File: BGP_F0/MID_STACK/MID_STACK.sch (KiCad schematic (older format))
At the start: 6 parts, among them P1 CONN_01X04, P2 CONN_01X09

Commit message: BT and MID pot gain ctrl reversed for proper action
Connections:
- net MID_I: now also P2.3 (P3); no longer P2.1 (P1)
- net MID_O: now also P2.1 (P1); no longer P2.3 (P3)
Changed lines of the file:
@@
 Comment4 ""
 $EndDescr
-Text Label 5500 3550 2    60   ~ 0
+Text Label 5500 3350 2    60   ~ 0
 VOL1
 Text Label 5500 3450 2    60   ~ 0
 VOL2
-Text Label 5500 3350 2    60   ~ 0
+Text Label 5500 3550 2    60   ~ 0
 VOL3
 Wire Wire Line

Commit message: Mid Buff
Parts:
- R1, R2: value 12k -> 6.8k
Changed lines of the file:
@@
 Text Label 5500 3550 2    60   ~ 0
 VOL3
-Wire Wire Line
-	5500 3450 5550 3450
 $Comp
 L C_Small C1
@@
 P 5900 3450
 F 0 "R1" H 5930 3470 50  0000 L CNN
-F 1 "12k" H 5930 3410 50  0000 L CNN
+F 1 "6.8k" H 5930 3410 50  0000 L CNN
 F 2 "Resistors_SMD:R_0603_HandSoldering" H 5900 3450 50  0001 C CNN
 F 3 "" H 5900 3450 50  0000 C CNN
@@
 	0    -1   -1   0
 $EndComp
-Wire Wire Line
-	5800 3450 5750 3450
-Wire Wire Line
-	6000 3450 6050 3450
 Text Label 6050 3450 3    60   ~ 0
 F1_2
 Text Label 6150 3450 3    60   ~ 0
 F1_1
-Wire Wire Line
-	6250 3450 6250 3900
-Wire Wire Line
-	6250 4000 6250 4050
 $Comp
 L R_Small R2
@@
 P 6250 4150
 F 0 "R2" H 6280 4170 50  0000 L CNN
-F 1 "12k" H 6280 4110 50  0000 L CNN
+F 1 "6.8k" H 6280 4110 50  0000 L CNN
 F 2 "Resistors_SMD:R_0603_HandSoldering" H 6250 4150 50  0001 C CNN
 F 3 "" H 6250 4150 50  0000 C CNN
@@
 	1    0    0    -1
 $EndComp
-Connection ~ 6250 3800
-Wire Wire Line
-	6250 4250 6250 4350
-Wire Wire Line
-	6250 4300 5950 4300
-Wire Wire Line
-	5950 4300 5950 4250
-Wire Wire Line
-	5950 4050 5950 3800
-Wire Wire Line
-	5950 3800 6250 3800
-Connection ~ 6250 4300
 Text Label 6900 3650 2    60   ~ 0
 VOL1
@@
 Text Label 6900 4350 2    60   ~ 0
 F2_2
-Wire Wire Line
-	6900 4150 6900 4050
-Wire Wire Line
-	6900 4450 6900 4350
-Wire Wire Line
-	6250 3450 6150 3450
-Wire Wire Line
-	5500 3200 5500 3350
-Wire Wire Line
-	5500 3650 5500 3550
 Text Label 6250 4350 3    60   ~ 0
 Vref
@@
 Text Label 5000 3900 0    60   ~ 0
 MID_I
+Wire Wire Line
+	5500 3450 5550 3450
+Wire Wire Line
+	5800 3450 5750 3450
+Wire Wire Line
+	6000 3450 6050 3450
+Wire Wire Line
+	6250 3450 6250 3900
+Wire Wire Line
+	6250 4000 6250 4050
+Connection ~ 6250 3800
+Wire Wire Line
+	6250 4250 6250 4350
+Wire Wire Line
+	6250 4300 5950 4300
+Wire Wire Line
+	5950 4300 5950 4250
+Wire Wire Line
+	5950 4050 5950 3800
+Wire Wire Line
+	5950 3800 6250 3800
+Connection ~ 6250 4300
+Wire Wire Line
+	6900 4150 6900 4050
+Wire Wire Line
+	6900 4450 6900 4350
+Wire Wire Line
+	6250 3450 6150 3450
+Wire Wire Line
+	5500 3200 5500 3350
+Wire Wire Line
+	5500 3650 5500 3550
 $EndSCHEMATC

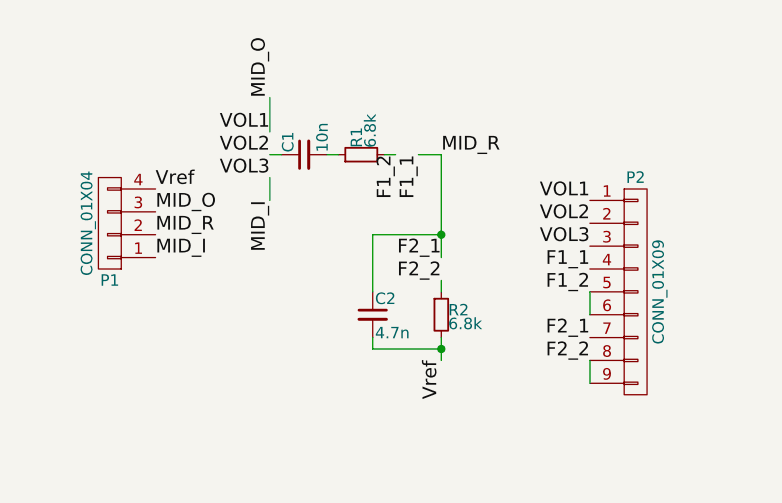
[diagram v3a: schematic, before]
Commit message: Change some caps to TH, updated BOM - need to recreate
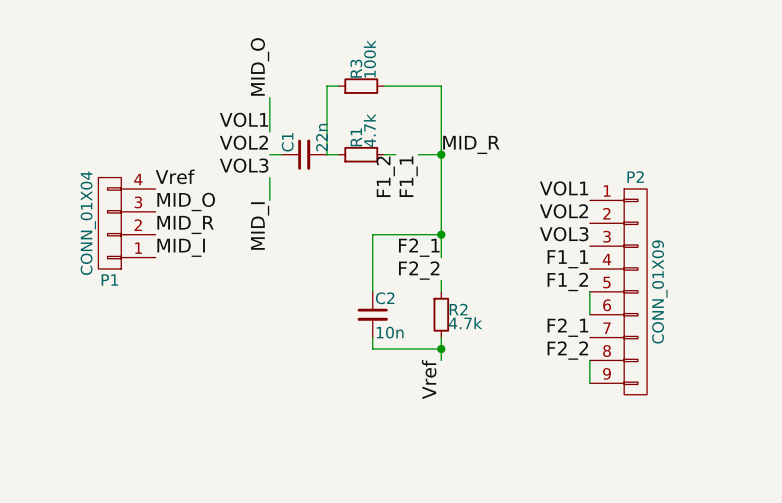
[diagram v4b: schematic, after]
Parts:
- added R3: 100k, Resistors_SMD:R_0603_HandSoldering, symbol R_Small
- C1: value 10n -> 22n; footprint Capacitors_SMD:C_0805_HandSoldering -> Capacitor_THT:C_Rect_L7.2mm_W2.5mm_P5.00mm_FKS2_FKP2_MKS2_MKP2
- C2: value 4.7n -> 10n; footprint Capacitors_SMD:C_0805_HandSoldering -> Capacitor_THT:C_Rect_L7.2mm_W2.5mm_P5.00mm_FKS2_FKP2_MKS2_MKP2
- R1, R2: value 6.8k -> 4.7k
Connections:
- net F1_1: now also R3.2
- net at C1.2, R1.1: now also R3.1
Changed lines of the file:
@@
 P 5650 3450
 F 0 "C1" H 5660 3520 50  0000 L CNN
-F 1 "10n" H 5660 3370 50  0000 L CNN
-F 2 "Capacitors_SMD:C_0805_HandSoldering" H 5650 3450 50  0001 C CNN
+F 1 "22n" H 5660 3370 50  0000 L CNN
+F 2 "Capacitor_THT:C_Rect_L7.2mm_W2.5mm_P5.00mm_FKS2_FKP2_MKS2_MKP2" H 5650 3450 50  0001 C CNN
 F 3 "" H 5650 3450 50  0000 C CNN
 	1    5650 3450
@@
 P 5900 3450
 F 0 "R1" H 5930 3470 50  0000 L CNN
-F 1 "6.8k" H 5930 3410 50  0000 L CNN
+F 1 "4.7k" H 5930 3410 50  0000 L CNN
 F 2 "Resistors_SMD:R_0603_HandSoldering" H 5900 3450 50  0001 C CNN
 F 3 "" H 5900 3450 50  0000 C CNN
@@
 P 6250 4150
 F 0 "R2" H 6280 4170 50  0000 L CNN
-F 1 "6.8k" H 6280 4110 50  0000 L CNN
+F 1 "4.7k" H 6280 4110 50  0000 L CNN
 F 2 "Resistors_SMD:R_0603_HandSoldering" H 6250 4150 50  0001 C CNN
 F 3 "" H 6250 4150 50  0000 C CNN
@@
 P 5950 4150
 F 0 "C2" H 5960 4220 50  0000 L CNN
-F 1 "4.7n" H 5960 4070 50  0000 L CNN
-F 2 "Capacitors_SMD:C_0805_HandSoldering" H 5950 4150 50  0001 C CNN
+F 1 "10n" H 5960 4070 50  0000 L CNN
+F 2 "Capacitor_THT:C_Rect_L7.2mm_W2.5mm_P5.00mm_FKS2_FKP2_MKS2_MKP2" H 5950 4150 50  0001 C CNN
 F 3 "" H 5950 4150 50  0000 C CNN
 	1    5950 4150
@@
 	6000 3450 6050 3450
 Wire Wire Line
-	6250 3450 6250 3900
+	6250 3150 6250 3900
 Wire Wire Line
 	6250 4000 6250 4050
@@
 Wire Wire Line
 	5500 3650 5500 3550
+$Comp
+L R_Small R3
+U 1 1 5A88CD87
+P 5900 3150
+F 0 "R3" H 5930 3170 50  0000 L CNN
+F 1 "100k" H 5930 3110 50  0000 L CNN
+F 2 "Resistors_SMD:R_0603_HandSoldering" H 5900 3150 50  0001 C CNN
+F 3 "" H 5900 3150 50  0000 C CNN
+	1    5900 3150
+	0    -1   -1   0
+$EndComp
+Wire Wire Line
+	5750 3450 5750 3150
+Wire Wire Line
+	5750 3150 5800 3150
+Wire Wire Line
+	6000 3150 6250 3150
+Connection ~ 6250 3450
 $EndSCHEMATC

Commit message: F0 Mid Stack fixed
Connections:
- net F1_1: now also P2.1 (P1); no longer P2.7 (P7)
- net F1_2: now also P2.2 (P2), P2.3 (P3); no longer P2.5 (P5), P2.6 (P6)
- net F2_2: now also P2.5 (P5), P2.6 (P6); no longer P2.8 (P8), P2.9 (P9)
- net MID_I: now also P2.9 (P9); no longer P2.3 (P3)
- net MID_O: now also P2.7 (P7); no longer P2.1 (P1)
- net VOL2: now also P2.8 (P8); no longer P2.2 (P2)
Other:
- moved on the sheet: P1, P2
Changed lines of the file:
@@
 	1    0    0    -1
 $EndComp
-Text Label 6900 3650 2    60   ~ 0
+Text Label 6950 3750 2    60   ~ 0
 VOL1
-Text Label 6900 3750 2    60   ~ 0
+Text Label 6950 3850 2    60   ~ 0
 VOL2
-Text Label 6900 3850 2    60   ~ 0
+Text Label 6950 3950 2    60   ~ 0
 VOL3
-Text Label 6900 3950 2    60   ~ 0
+Text Label 6950 3150 2    60   ~ 0
 F1_1
-Text Label 6900 4050 2    60   ~ 0
+Text Label 6950 3250 2    60   ~ 0
 F1_2
-Text Label 6900 4250 2    60   ~ 0
+Text Label 6950 3450 2    60   ~ 0
 F2_1
-Text Label 6900 4350 2    60   ~ 0
+Text Label 6950 3550 2    60   ~ 0
 F2_2
 Text Label 6250 4350 3    60   ~ 0
@@
 L CONN_01X09 P2
 U 1 1 5A669FB9
-P 7100 4050
-F 0 "P2" H 7100 4550 50  0000 C CNN
-F 1 "CONN_01X09" V 7200 4050 50  0000 C CNN
-F 2 "LIBS:Potentiometer_Alpha_Tripple_Vertical_Dual_Shaft" H 7100 4050 50  0001 C CNN
-F 3 "" H 7100 4050 50  0000 C CNN
-	1    7100 4050
+P 7150 3550
+F 0 "P2" H 7150 4050 50  0000 C CNN
+F 1 "CONN_01X09" V 7250 3550 50  0000 C CNN
+F 2 "LIBS:Potentiometer_Alpha_Tripple_Vertical_Dual_Shaft" H 7150 3550 50  0001 C CNN
+F 3 "" H 7150 3550 50  0000 C CNN
+	1    7150 3550
 	1    0    0    -1
 $EndComp
@@
 L CONN_01X04 P1
 U 1 1 5A66A01B
-P 4800 3750
-F 0 "P1" H 4800 4000 50  0000 C CNN
-F 1 "CONN_01X04" V 4900 3750 50  0000 C CNN
-F 2 "Connectors_JST:JST_PH_B4B-PH-K_04x2.00mm_Straight" H 4800 3750 50  0001 C CNN
-F 3 "" H 4800 3750 50  0000 C CNN
-	1    4800 3750
+P 4550 3300
+F 0 "P1" H 4550 3550 50  0000 C CNN
+F 1 "CONN_01X04" V 4650 3300 50  0000 C CNN
+F 2 "Connectors_JST:JST_PH_B4B-PH-K_04x2.00mm_Straight" H 4550 3300 50  0001 C CNN
+F 3 "" H 4550 3300 50  0000 C CNN
+	1    4550 3300
 	-1   0    0    1
 $EndComp
-Text Label 5000 3600 0    60   ~ 0
+Text Label 4750 3150 0    60   ~ 0
 Vref
-Text Label 5000 3700 0    60   ~ 0
+Text Label 4750 3250 0    60   ~ 0
 MID_O
-Text Label 5000 3800 0    60   ~ 0
+Text Label 4750 3350 0    60   ~ 0
 MID_R
-Text Label 5000 3900 0    60   ~ 0
+Text Label 4750 3450 0    60   ~ 0
 MID_I
 Wire Wire Line
@@
 Connection ~ 6250 4300
 Wire Wire Line
-	6900 4150 6900 4050
+	6950 3350 6950 3250
 Wire Wire Line
-	6900 4450 6900 4350
+	6950 3650 6950 3550
 Wire Wire Line
 	6250 3450 6150 3450

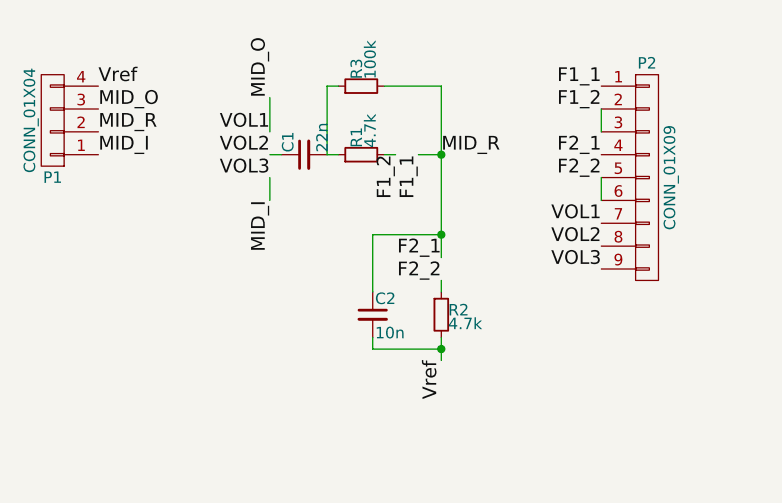
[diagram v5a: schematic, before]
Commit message: F0 Pot Wiring reversed after testing
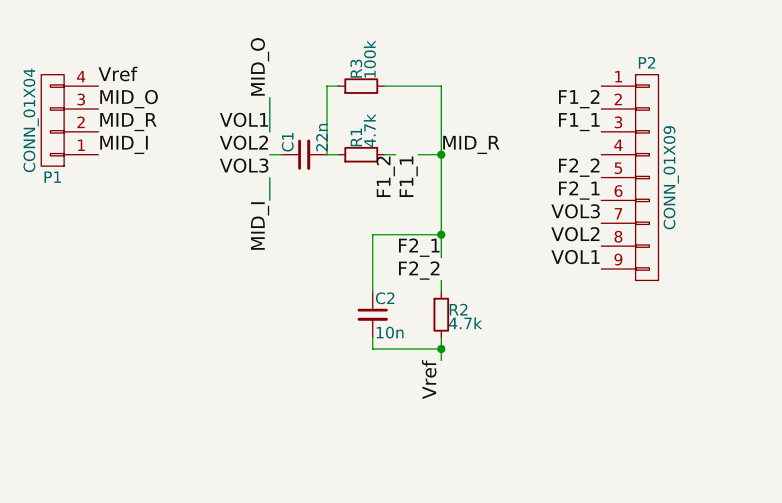
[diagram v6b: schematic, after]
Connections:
- net F1_1: now also P2.3 (P3), P2.6 (P6); no longer P2.1 (P1), P2.4 (P4)
- net F1_2: no longer P2.3 (P3)
- net F2_2: no longer P2.6 (P6)
- net MID_I: now also P2.7 (P7); no longer P2.9 (P9)
- net MID_O: now also P2.9 (P9); no longer P2.7 (P7)
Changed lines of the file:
@@
 	1    0    0    -1
 $EndComp
-Text Label 6950 3750 2    60   ~ 0
+Text Label 6950 3950 2    60   ~ 0
 VOL1
 Text Label 6950 3850 2    60   ~ 0
 VOL2
-Text Label 6950 3950 2    60   ~ 0
+Text Label 6950 3750 2    60   ~ 0
 VOL3
-Text Label 6950 3150 2    60   ~ 0
+Text Label 6950 3350 2    60   ~ 0
 F1_1
 Text Label 6950 3250 2    60   ~ 0
 F1_2
-Text Label 6950 3450 2    60   ~ 0
+Text Label 6950 3650 2    60   ~ 0
 F2_1
 Text Label 6950 3550 2    60   ~ 0
@@
 Connection ~ 6250 4300
 Wire Wire Line
-	6950 3350 6950 3250
-Wire Wire Line
-	6950 3650 6950 3550
-Wire Wire Line
 	6250 3450 6150 3450

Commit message: F0 - Fixed Mid Stack, BT, BUF
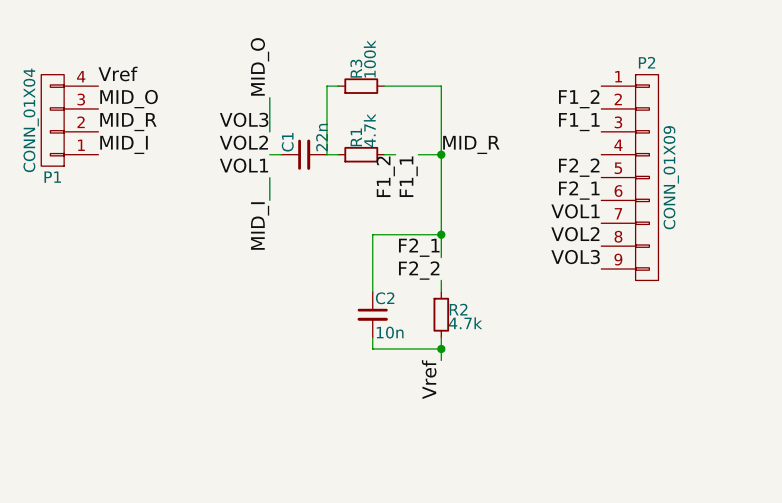
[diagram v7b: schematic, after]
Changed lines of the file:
@@
 Comment4 ""
 $EndDescr
-Text Label 5500 3350 2    60   ~ 0
+Text Label 5500 3550 2    60   ~ 0
 VOL1
 Text Label 5500 3450 2    60   ~ 0
 VOL2
-Text Label 5500 3550 2    60   ~ 0
+Text Label 5500 3350 2    60   ~ 0
 VOL3
 $Comp
@@
 	1    0    0    -1
 $EndComp
-Text Label 6950 3950 2    60   ~ 0
+Text Label 6950 3750 2    60   ~ 0
 VOL1
 Text Label 6950 3850 2    60   ~ 0
 VOL2
-Text Label 6950 3750 2    60   ~ 0
+Text Label 6950 3950 2    60   ~ 0
 VOL3
 Text Label 6950 3350 2    60   ~ 0

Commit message: MM Gerbers Finished, Mid Stack Ammended J0
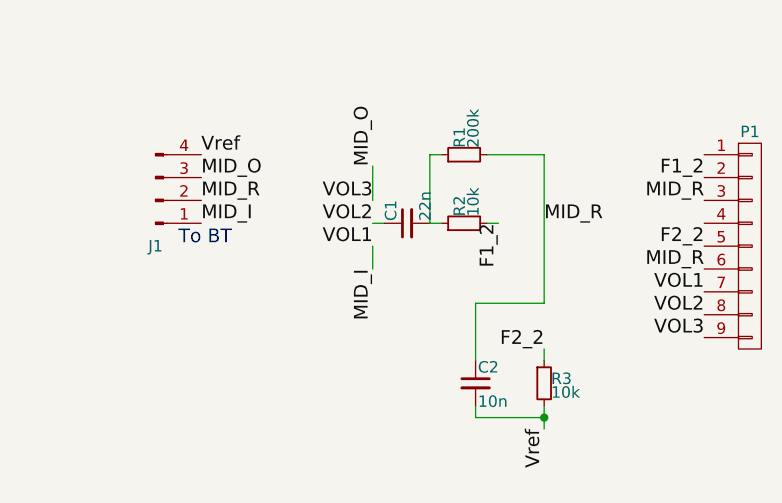
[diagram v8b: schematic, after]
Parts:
- removed P1: CONN_01X04, Connectors_JST:JST_PH_B4B-PH-K_04x2.00mm_Straight, symbol CONN_01X04
- added J1: Conn_01x04_Male, Connectors_JST:JST_PH_B4B-PH-K_04x2.00mm_Straight, symbol Conn_01x04_Male
- C1: footprint Capacitor_THT:C_Rect_L7.2mm_W2.5mm_P5.00mm_FKS2_FKP2_MKS2_MKP2 -> Capacitors_SMD:C_1206
- C2: footprint Capacitor_THT:C_Rect_L7.2mm_W2.5mm_P5.00mm_FKS2_FKP2_MKS2_MKP2 -> Capacitors_SMD:C_0805
- R1: renamed from R3; value 100k -> 200k
- R2: renamed from R1; value 4.7k -> 10k
- R3: renamed from R2; value 4.7k -> 10k
- renumbered P2 to P1
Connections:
- net MID_I: now also J1.1 (Pin_1)
- net MID_O: now also J1.3 (Pin_3)
- net Vref: now also J1.4 (Pin_4)
- net F1_1 renamed MID_R
- net MID_R: now also J1.2 (Pin_2)
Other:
- note added: "To BT"
- moved on the sheet: C1, C2, P1, R1, R2, R3
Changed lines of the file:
@@
 Comment4 ""
 $EndDescr
-Text Label 5500 3550 2    60   ~ 0
+Text Label 5950 3850 2    60   ~ 0
 VOL1
-Text Label 5500 3450 2    60   ~ 0
+Text Label 5950 3750 2    60   ~ 0
 VOL2
-Text Label 5500 3350 2    60   ~ 0
+Text Label 5950 3650 2    60   ~ 0
 VOL3
 $Comp
 L C_Small C1
 U 1 1 5A4C54B9
-P 5650 3450
-F 0 "C1" H 5660 3520 50  0000 L CNN
-F 1 "22n" H 5660 3370 50  0000 L CNN
-F 2 "Capacitor_THT:C_Rect_L7.2mm_W2.5mm_P5.00mm_FKS2_FKP2_MKS2_MKP2" H 5650 3450 50  0001 C CNN
-F 3 "" H 5650 3450 50  0000 C CNN
-	1    5650 3450
+P 6100 3750
+F 0 "C1" H 6110 3820 50  0000 L CNN
+F 1 "22n" H 6110 3670 50  0000 L CNN
+F 2 "Capacitors_SMD:C_1206" H 6100 3750 50  0001 C CNN
+F 3 "" H 6100 3750 50  0000 C CNN
+	1    6100 3750
 	0    -1   -1   0
 $EndComp
 $Comp
-L R_Small R1
+L R_Small R2
 U 1 1 5A4C5562
-P 5900 3450
-F 0 "R1" H 5930 3470 50  0000 L CNN
-F 1 "4.7k" H 5930 3410 50  0000 L CNN
-F 2 "Resistors_SMD:R_0603_HandSoldering" H 5900 3450 50  0001 C CNN
-F 3 "" H 5900 3450 50  0000 C CNN
-	1    5900 3450
+P 6350 3750
+F 0 "R2" H 6380 3770 50  0000 L CNN
+F 1 "10k" H 6380 3710 50  0000 L CNN
+F 2 "Resistors_SMD:R_0603_HandSoldering" H 6350 3750 50  0001 C CNN
+F 3 "" H 6350 3750 50  0000 C CNN
+	1    6350 3750
 	0    -1   -1   0
 $EndComp
-Text Label 6050 3450 3    60   ~ 0
+Text Label 6500 3750 3    60   ~ 0
 F1_2
-Text Label 6150 3450 3    60   ~ 0
-F1_1
 $Comp
-L R_Small R2
+L R_Small R3
 U 1 1 5A4C5B1B
-P 6250 4150
-F 0 "R2" H 6280 4170 50  0000 L CNN
-F 1 "4.7k" H 6280 4110 50  0000 L CNN
-F 2 "Resistors_SMD:R_0603_HandSoldering" H 6250 4150 50  0001 C CNN
-F 3 "" H 6250 4150 50  0000 C CNN
-	1    6250 4150
+P 6700 4450
+F 0 "R3" H 6730 4470 50  0000 L CNN
+F 1 "10k" H 6730 4410 50  0000 L CNN
+F 2 "Resistors_SMD:R_0603_HandSoldering" H 6700 4450 50  0001 C CNN
+F 3 "" H 6700 4450 50  0000 C CNN
+	1    6700 4450
 	1    0    0    -1
 $EndComp
-Text Label 6250 3900 2    60   ~ 0
-F2_1
-Text Label 6250 4000 2    60   ~ 0
+Text Label 6700 4300 2    60   ~ 0
 F2_2
 $Comp
 L C_Small C2
 U 1 1 5A4C5BAB
-P 5950 4150
-F 0 "C2" H 5960 4220 50  0000 L CNN
-F 1 "10n" H 5960 4070 50  0000 L CNN
-F 2 "Capacitor_THT:C_Rect_L7.2mm_W2.5mm_P5.00mm_FKS2_FKP2_MKS2_MKP2" H 5950 4150 50  0001 C CNN
-F 3 "" H 5950 4150 50  0000 C CNN
-	1    5950 4150
+P 6400 4450
+F 0 "C2" H 6410 4520 50  0000 L CNN
+F 1 "10n" H 6410 4370 50  0000 L CNN
+F 2 "Capacitors_SMD:C_0805" H 6400 4450 50  0001 C CNN
+F 3 "" H 6400 4450 50  0000 C CNN
+	1    6400 4450
 	1    0    0    -1
 $EndComp
-Text Label 6950 3750 2    60   ~ 0
+Text Label 7400 4050 2    60   ~ 0
 VOL1
-Text Label 6950 3850 2    60   ~ 0
+Text Label 7400 4150 2    60   ~ 0
 VOL2
-Text Label 6950 3950 2    60   ~ 0
+Text Label 7400 4250 2    60   ~ 0
 VOL3
-Text Label 6950 3350 2    60   ~ 0
-F1_1
-Text Label 6950 3250 2    60   ~ 0
+Text Label 7400 3550 2    60   ~ 0
 F1_2
-Text Label 6950 3650 2    60   ~ 0
-F2_1
-Text Label 6950 3550 2    60   ~ 0
+Text Label 7400 3850 2    60   ~ 0
 F2_2
-Text Label 6250 4350 3    60   ~ 0
+Text Label 6700 4650 3    60   ~ 0
 Vref
-Text Label 5500 3200 1    60   ~ 0
+Text Label 5950 3500 1    60   ~ 0
 MID_O
-Text Label 5500 3650 3    60   ~ 0
+Text Label 5950 3950 3    60   ~ 0
 MID_I
-Text Label 6250 3450 0    60   ~ 0
+Text Label 6700 3750 0    60   ~ 0
 MID_R
 $Comp
-L CONN_01X09 P2
+L CONN_01X09 P1
 U 1 1 5A669FB9
-P 7150 3550
-F 0 "P2" H 7150 4050 50  0000 C CNN
-F 1 "CONN_01X09" V 7250 3550 50  0000 C CNN
-F 2 "LIBS:Potentiometer_Alpha_Tripple_Vertical_Dual_Shaft" H 7150 3550 50  0001 C CNN
-F 3 "" H 7150 3550 50  0000 C CNN
-	1    7150 3550
+P 7600 3850
+F 0 "P1" H 7600 4350 50  0000 C CNN
+F 1 "CONN_01X09" V 7700 3850 50  0001 C CNN
+F 2 "LIBS:Potentiometer_Alpha_Tripple_Vertical_Dual_Shaft" H 7600 3850 50  0001 C CNN
+F 3 "" H 7600 3850 50  0000 C CNN
+	1    7600 3850
 	1    0    0    -1
 $EndComp
-$Comp
-L CONN_01X04 P1
-U 1 1 5A66A01B
-P 4550 3300
-F 0 "P1" H 4550 3550 50  0000 C CNN
-F 1 "CONN_01X04" V 4650 3300 50  0000 C CNN
-F 2 "Connectors_JST:JST_PH_B4B-PH-K_04x2.00mm_Straight" H 4550 3300 50  0001 C CNN
-F 3 "" H 4550 3300 50  0000 C CNN
-	1    4550 3300
-	-1   0    0    1
-$EndComp
-Text Label 4750 3150 0    60   ~ 0
+Text Label 5200 3450 0    60   ~ 0
 Vref
-Text Label 4750 3250 0    60   ~ 0
+Text Label 5200 3550 0    60   ~ 0
 MID_O
-Text Label 4750 3350 0    60   ~ 0
+Text Label 5200 3650 0    60   ~ 0
 MID_R
-Text Label 4750 3450 0    60   ~ 0
+Text Label 5200 3750 0    60   ~ 0
 MID_I
 Wire Wire Line
-	5500 3450 5550 3450
+	5950 3750 6000 3750
 Wire Wire Line
-	5800 3450 5750 3450
+	6250 3750 6200 3750
 Wire Wire Line
-	6000 3450 6050 3450
+	6450 3750 6500 3750
 Wire Wire Line
-	6250 3150 6250 3900
+	6700 4300 6700 4350
 Wire Wire Line
-	6250 4000 6250 4050
-Connection ~ 6250 3800
+	6700 4550 6700 4650
 Wire Wire Line
-	6250 4250 6250 4350
+	6700 4600 6400 4600
 Wire Wire Line
-	6250 4300 5950 4300
+	6400 4600 6400 4550
 Wire Wire Line
-	5950 4300 5950 4250
+	6400 4350 6400 4100
 Wire Wire Line
-	5950 4050 5950 3800
+	6400 4100 6700 4100
+Connection ~ 6700 4600
 Wire Wire Line
-	5950 3800 6250 3800
-Connection ~ 6250 4300
+	5950 3500 5950 3650
 Wire Wire Line
-	6250 3450 6150 3450
-Wire Wire Line
-	5500 3200 5500 3350
-Wire Wire Line
-	5500 3650 5500 3550
+	5950 3950 5950 3850
 $Comp
-L R_Small R3
+L R_Small R1
 U 1 1 5A88CD87
-P 5900 3150
-F 0 "R3" H 5930 3170 50  0000 L CNN
-F 1 "100k" H 5930 3110 50  0000 L CNN
-F 2 "Resistors_SMD:R_0603_HandSoldering" H 5900 3150 50  0001 C CNN
-F 3 "" H 5900 3150 50  0000 C CNN
-	1    5900 3150
+P 6350 3450
+F 0 "R1" H 6380 3470 50  0000 L CNN
+F 1 "200k" H 6380 3410 50  0000 L CNN
+F 2 "Resistors_SMD:R_0603_HandSoldering" H 6350 3450 50  0001 C CNN
+F 3 "" H 6350 3450 50  0000 C CNN
+	1    6350 3450
 	0    -1   -1   0
 $EndComp
 Wire Wire Line
-	5750 3450 5750 3150
+	6200 3750 6200 3450
 Wire Wire Line
-	5750 3150 5800 3150
+	6200 3450 6250 3450
 Wire Wire Line
-	6000 3150 6250 3150
-Connection ~ 6250 3450
+	6450 3450 6700 3450
+Text Notes 5100 3850 0    60   ~ 0
+To BT
+$Comp
+L Conn_01x04_Male J1
+U 1 1 5B03DCA0
+P 5000 3650
+F 0 "J1" H 5000 3850 50  0000 C CNN
+F 1 "Conn_01x04_Male" H 5000 3350 50  0001 C CNN
+F 2 "Connectors_JST:JST_PH_B4B-PH-K_04x2.00mm_Straight" H 5000 3650 50  0001 C CNN
+F 3 "" H 5000 3650 50  0001 C CNN
+	1    5000 3650
+	1    0    0    1
+$EndComp
+Text Label 7400 3950 2    60   ~ 0
+MID_R
+Text Label 7400 3650 2    60   ~ 0
+MID_R
+Wire Wire Line
+	6700 3450 6700 4100
 $EndSCHEMATC
